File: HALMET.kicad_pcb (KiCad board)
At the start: 4 copper layers, 89 x 58 mm, 248 parts, among them J1103 Conn_01x02, J1104 Conn_01x02, J1105 Conn_01x02, J1106 Conn_01x02, J1201 Conn_01x02, J201 GPIO, J203 Conn_01x01, J302 Conn_01x02, J401 USB_B_Micro, J402 Conn_01x04, J501 EXT LEDS, J602 Conn_02x04_Odd_Even, J604 Conn_01x02, J605 Conn_01x02, J606 Conn_01x02, J607 Conn_01x02, J702 Conn_01x04, J801 Conn_01x03, J802 Conn_01x04, Q401 S8050, Q402 S8050, Q601 BC856BW,115, Q602 BC856BW,115, Q603 BC856BW,115, Q604 BC856BW,115, SW501 SW_Push, SW502 SW_Push, U1101 74LVC1G17, U1102 74LVC1G17, U1103 74LVC1G17, U1104 74LVC1G17, U1200 ICM-42688-P, U1201 π140U30, U1202 ISO1540, U1203 XC6206P332MR, U201 ESP32-S3-WROOM-1U-N16R2, U202 XL1509-3.3, U203 LM317L_SOT-89, U401 CH340C, U501 SN65HVD230DR, U502 SP3485EN, U601 LMV324, U602 ADS1115IDGS

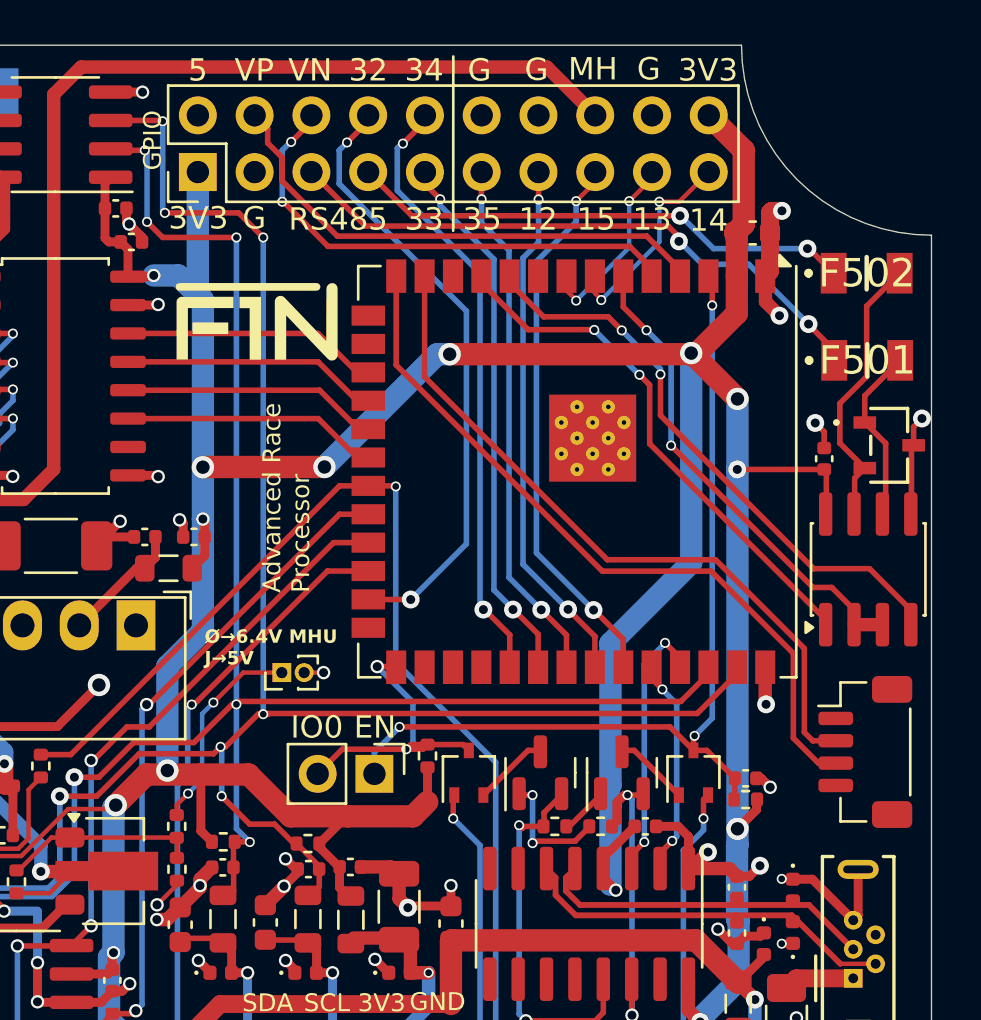
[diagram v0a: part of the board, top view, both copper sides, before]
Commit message: Added TSV/ESD to the native USB
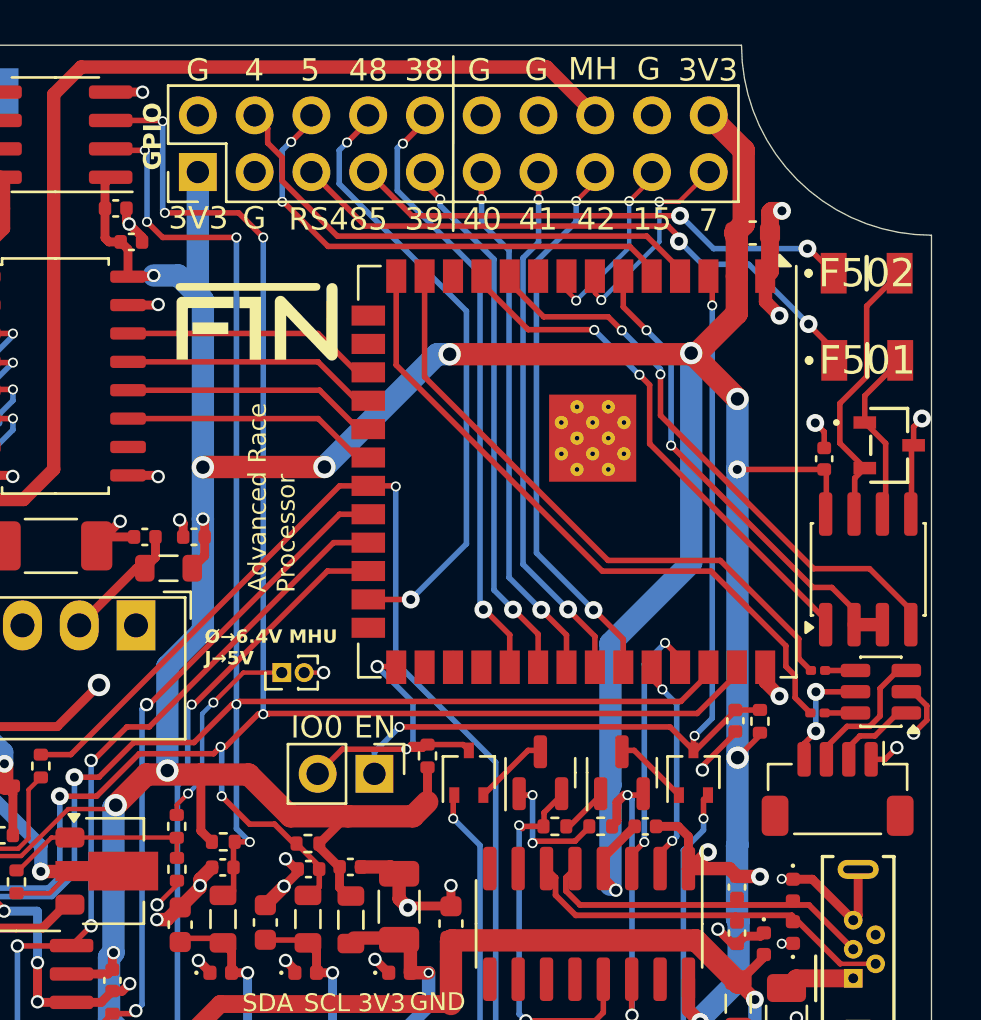
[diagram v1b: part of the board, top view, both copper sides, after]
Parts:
- added R403: 27R, Resistor_SMD:R_0201_0603Metric, F.Cu at (172.9, 86.9)
- added R404: 27R, Resistor_SMD:R_0201_0603Metric, F.Cu at (172.9, 85.0)
- added U402: USBLC6-2SC6, Package_TO_SOT_SMD:SOT-23-6, F.Cu at (175.7, 85.9)
- moved R201 3.56 mm to (170.3, 87.2), turned to 90 degrees
- moved C203 2.62 mm to (169.2, 87.2), turned to -90 degrees
- moved J402 2.07 mm to (173.8, 90.3), turned to 180 degrees
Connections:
- J402 pad 1: unconnected-(J402-Pin_1-Pad1) -> GND
- J402 pad 2: /USB_D_MINUS -> /USB/USB_CONN_DP
- J402 pad 3: /USB_D_PLUS -> /USB/USB_CONN_DM
- J402 pad 4: unconnected-(J402-Pin_4-Pad4) -> /USB/USB_VBUS
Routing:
- net /USB/USB_CONN_DM: track 0.00 -> 6.27 mm
- net GND: track 160.3 -> 165.6 mm, vias 76 -> 78
- net /USB/USB_VBUS: track 0.00 -> 5.08 mm, vias 0 -> 2
- net /USB_D_MINUS: track 31.8 -> 27.8 mm
- net /USB/USB_CONN_DP: track 0.00 -> 3.91 mm
- net /USB_D_PLUS: track 33.2 -> 30.1 mm
- net Net-(R403-Pad1): track 0.00 -> 1.38 mm
- net Net-(R404-Pad1): track 0.00 -> 1.35 mm
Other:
- board text added: "38"
- board text added: "39"
- board text added: "4"
- board text added: "40"
- board text added: "41"
- board text added: "42"
- board text added: "48"
- board text added: "7"
- board text removed: "12"
- board text removed: "13"
- board text removed: "14"
- board text removed: "32"
- board text removed: "33"
- board text removed: "34"
- board text removed: "35"
- board text removed: "VN"
- board text removed: "VP"

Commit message: Silkscreen updates
Back silkscreen bough up-to-date with GPIO pin changes
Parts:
- moved G602 3.26 mm to (156.6, 70.8)
- moved REF** 3.26 mm to (167.6, 71.7)
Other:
- board text added: "01 SCL"
- board text added: "02 SDA"
- board text added: "06 RS485_IO"
- board text added: "09 DI1"
- board text added: "10 DI2"
- board text added: "11 DI3"
- board text added: "12 DI4"
- board text added: "13 LED"
- board text added: "14 CAN_TX"
- board text added: "17 RS485_TX"
- board text added: "18 RS485_RX"
- board text added: "19 USB_D-"
- board text added: "20 USB_D+"
- board text added: "21 CAN_RX"
- board text added: "39 TCK"
- board text added: "40 TDO"
- board text added: "41 TDI"
- board text added: "42 TMS"
- board text added: "43 USB_UART_TX"
- board text added: "44 USB_UART_RX"
- board text added: "47 1WIRE-DQ"
- board text added: "N2K Term"
- board text removed: "01 TXD0"
- board text removed: "02 LED"
- board text removed: "03 RXD0"
- board text removed: "04 1-WIRE"
- board text removed: "12 TDI"
- board text removed: "13 TCK"
- board text removed: "14 TMS"
- board text removed: "15 TDO"
- board text removed: "18 CAN_RX"
- board text removed: "19 CAN_TX"
- board text removed: "21 SDA"
- board text removed: "22 SCL"
- board text removed: "23 DI1"
- board text removed: "25 DI2"
- board text removed: "26 DI4"
- board text removed: "27 DI3"
- board text removed: "CAN term."
